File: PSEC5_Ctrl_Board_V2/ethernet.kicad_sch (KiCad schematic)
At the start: 46 parts, among them Q6 NMOS, Q8 NMOS, T1 7499111446, U1 88E1512-A0-NNP2C000, Y3 ASE2-25.000MHZ-ET

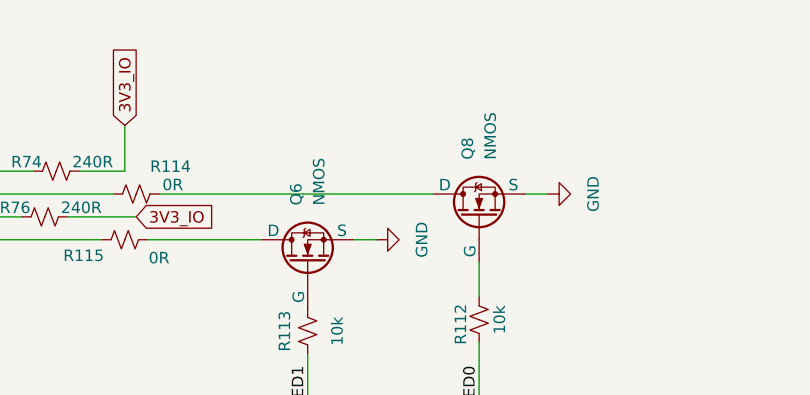
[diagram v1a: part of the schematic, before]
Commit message: Adjusted Footprints
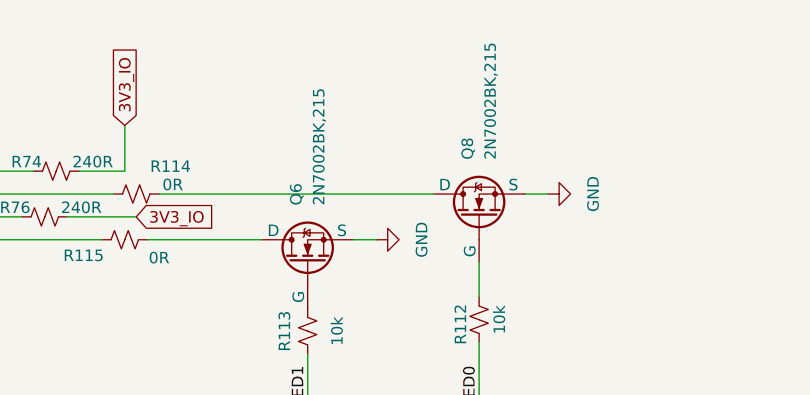
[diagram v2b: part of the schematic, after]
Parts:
- C59: footprint Capacitor_SMD:C_0603_1608Metric -> Capacitor_SMD:C_0805_2012Metric
- L3: footprint Resistor_SMD:R_0603_1608Metric -> Resistor_SMD:R_0402_1005Metric
- Q6, Q8: value NMOS -> 2N7002BK,215
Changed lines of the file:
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@@
 			)
 		)
-		(property "Footprint" "Capacitor_SMD:C_0603_1608Metric"
+		(property "Footprint" "Capacitor_SMD:C_0805_2012Metric"
 			(at 209.2452 140.97 0)
 			(effects
@@
 			)
 		)
-		(property "Value" "NMOS"
+		(property "Value" "2N7002BK,215"
 			(at 196.8499 31.75 0)
 			(effects
@@
 			)
 		)
-		(property "Value" "NMOS"
+		(property "Value" "2N7002BK,215"
 			(at 215.8999 26.67 0)
 			(effects
@@
 			)
 		)
-		(property "Footprint" "Resistor_SMD:R_0603_1608Metric"
+		(property "Footprint" "Resistor_SMD:R_0402_1005Metric"
 			(at 57.15 128.27 0)
 			(effects

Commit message: Updated kria
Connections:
- net 3V3_IO: no longer C61.1, C63.1, U1.10 (VDDO_SEL), U1.11 (VDDO), U1.49 (VDDO), U1.52 (VDDO)
- new net 1V8_Banks: C61.1, C63.1, U1.10 (VDDO_SEL), U1.11 (VDDO), U1.49 (VDDO), U1.52 (VDDO)
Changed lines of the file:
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@@
 		)
 	)
-	(global_label "3V3_IO"
+	(global_label "1V8_Banks"
 		(shape input)
 		(at 59.69 95.25 0)
@@
 		)
 		(property "Intersheetrefs" "${INTERSHEET_REFS}"
-			(at 69.0857 95.25 0)
+			(at 72.7746 95.25 0)
 			(effects
 				(font
+					(size 1.27 1.27)
+				)
+				(justify left)
+				(hide yes)
+			)
+		)
+		(property "Netclass" ""
+			(at 59.69 97.4408 0)
+			(effects
+				(font

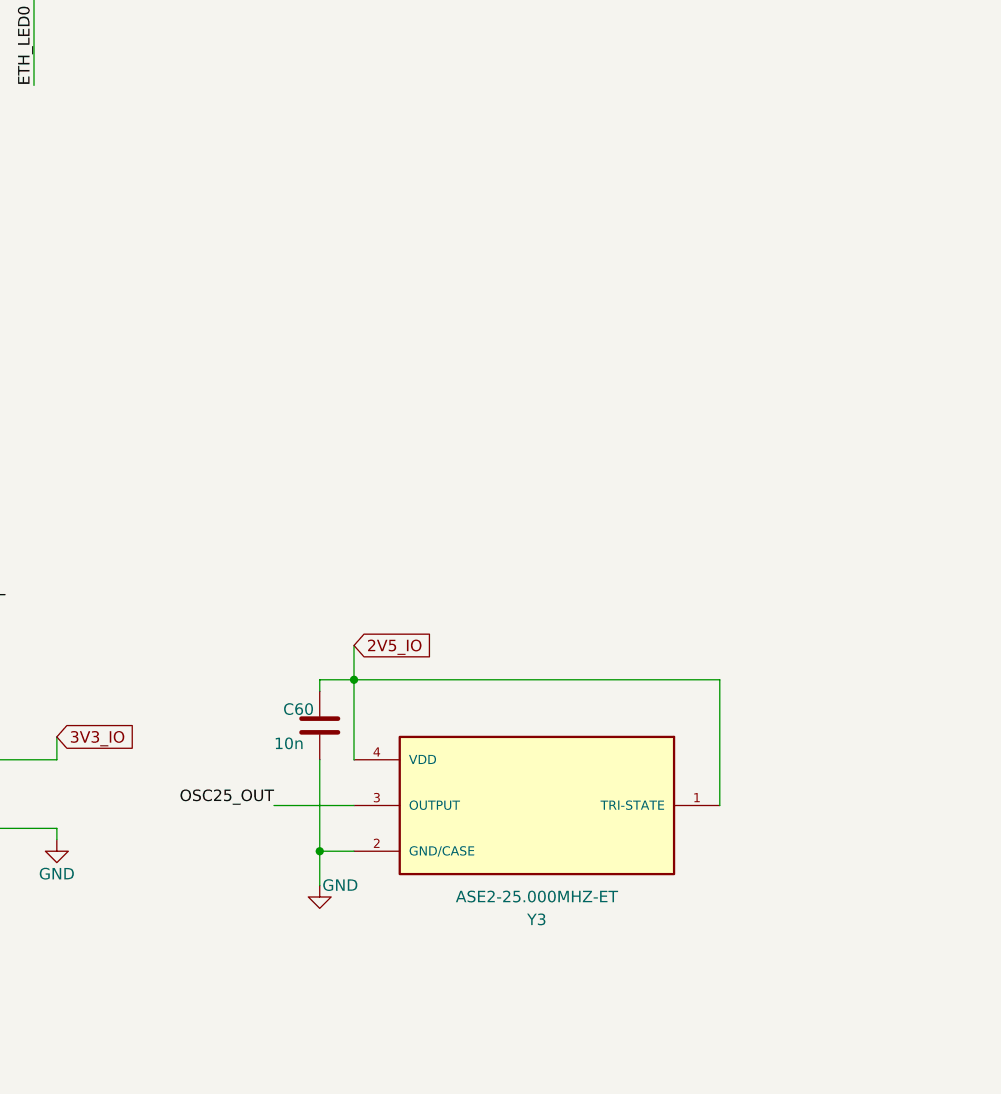
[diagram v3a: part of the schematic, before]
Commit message: Updated Joes Initial Comments. Schematic should be functional
Fixed Joes comments. Still discrepancy on the inversion signal during Voltage Handshake. However, added inverter signal that we can turn on or off depending on what is desired.
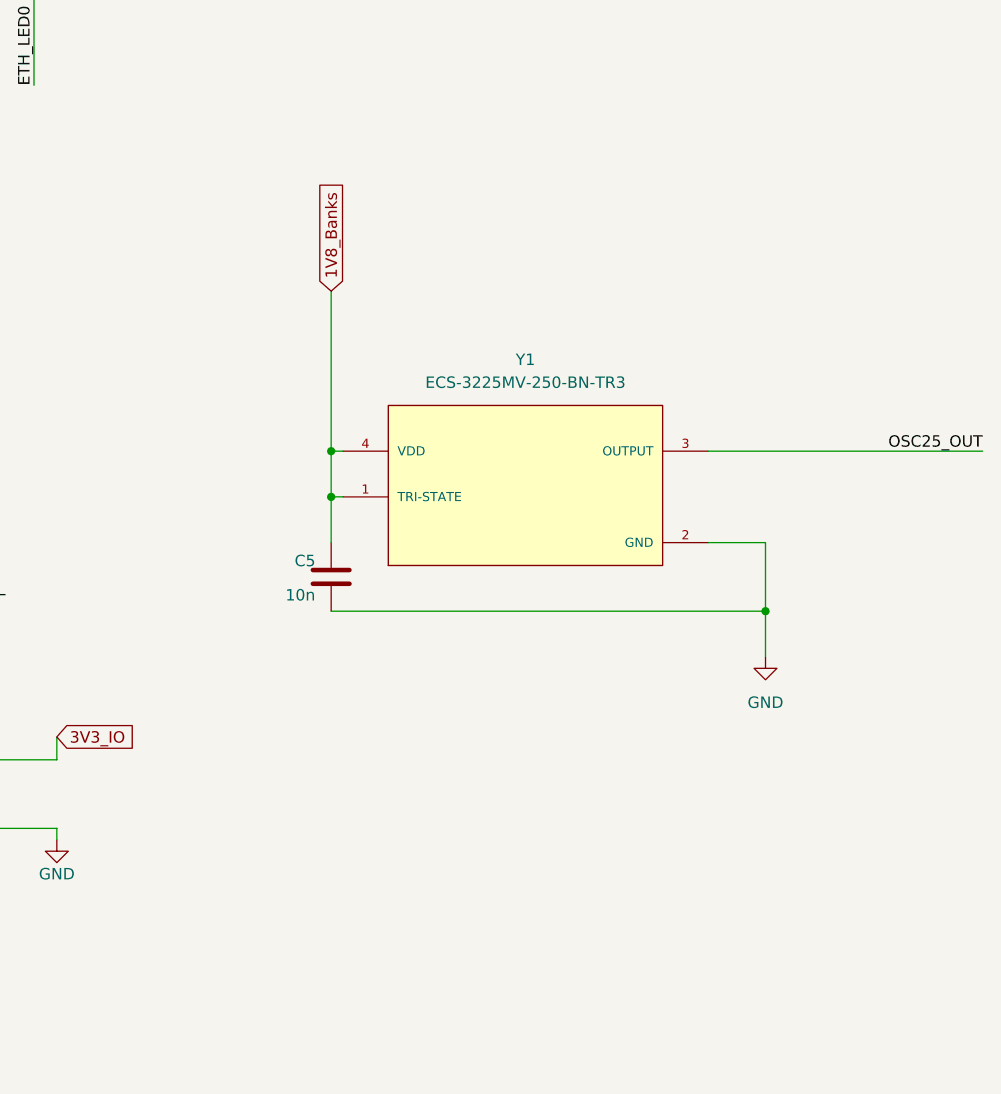
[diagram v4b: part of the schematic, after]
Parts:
- removed C60: 10n, Capacitor_SMD:C_0603_1608Metric, symbol Device:C
- removed Y3: ASE2-25.000MHZ-ET, ASE2_25_000MHZ_ET:XTAL_ASE2-25.000MHZ-ET, symbol PSEC5_ctrlbd:ASE2-25.000MHZ-ET
- added C5: 10n, Capacitor_SMD:C_0603_1608Metric, symbol Device:C
- added Y1: ECS-3225MV-250-BN-TR3, ECS-3225MV-250-BN-TR3:OSC_ECS-2333-160-BN-TR, symbol Oscillator:ECS-3225MV-250-BN-TR3
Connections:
- net 1V8_Banks: now also C5.1, Y1.1 (TRI-STATE), Y1.4 (VDD)
- net GND: now also C5.2, Y1.2 (GND)
- net OSC25_OUT: now also Y1.3 (OUTPUT)
